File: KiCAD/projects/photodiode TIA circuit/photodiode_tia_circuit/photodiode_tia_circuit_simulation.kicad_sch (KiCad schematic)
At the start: 8 parts, among them U2 ${SIM.PARAMS}, U3 ${SIM.PARAMS}

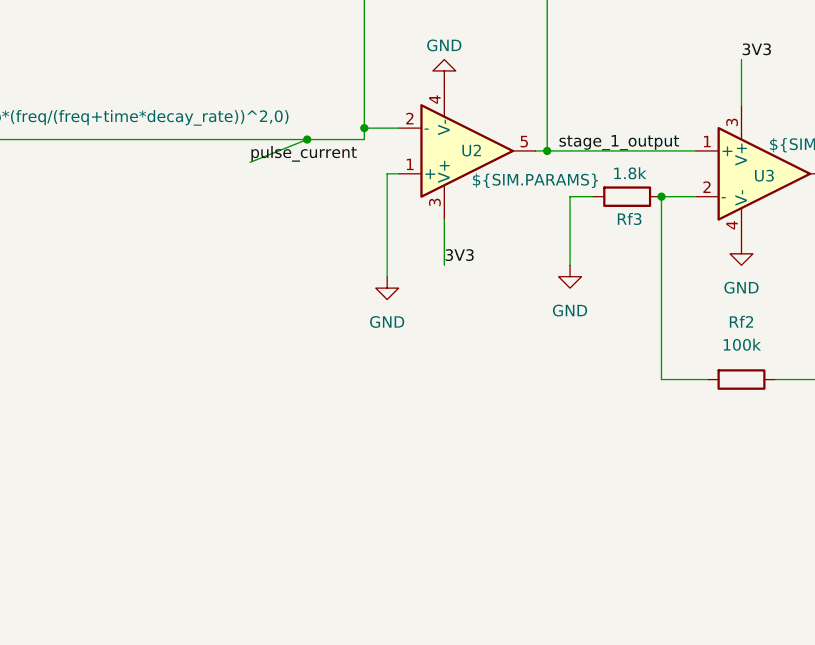
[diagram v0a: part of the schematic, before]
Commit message: removed history tracking
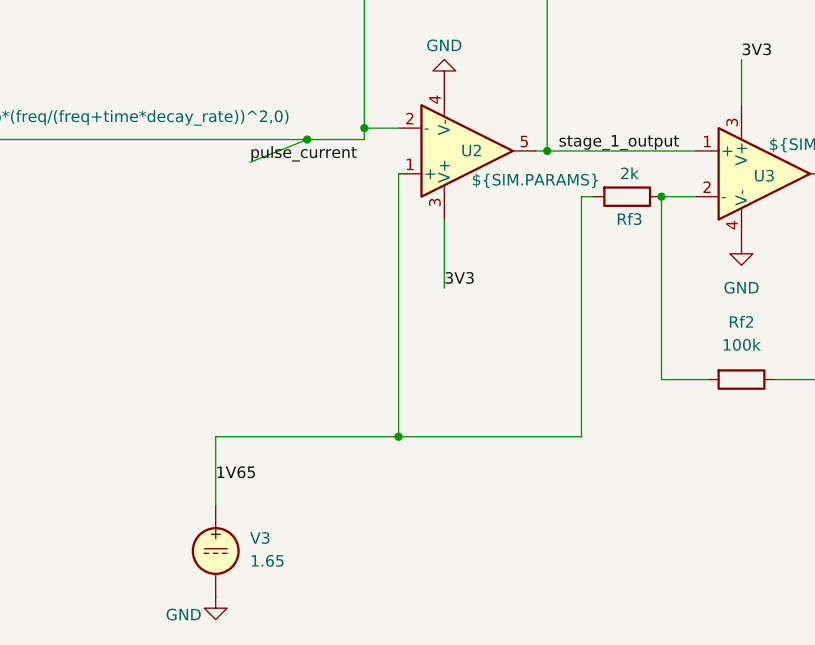
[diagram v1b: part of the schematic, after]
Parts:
- added V3: 1.65, symbol Simulation_SPICE:VDC
- Rf3: value 1.8k -> 2k
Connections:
- net GND: now also V3.2; no longer Rf3.2, U2.1 (+)
- new net 1V65: Rf3.2, U2.1 (+), V3.1
